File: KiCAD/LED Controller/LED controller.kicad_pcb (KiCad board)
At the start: 2 copper layers, 100 x 100 mm, 35 parts, among them J1 Barrel_Jack_Switch, J2 4x RJ45, SW1 ELUMOASAQ2C22, SW2 ELUMOASAQ2C22, SW3 ELUMOASAQ2C22, U1 SN75374D, U2 SN75374D, U3 Teensy4.1, U4 SN75374D, U5 SN74LV4053ADR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

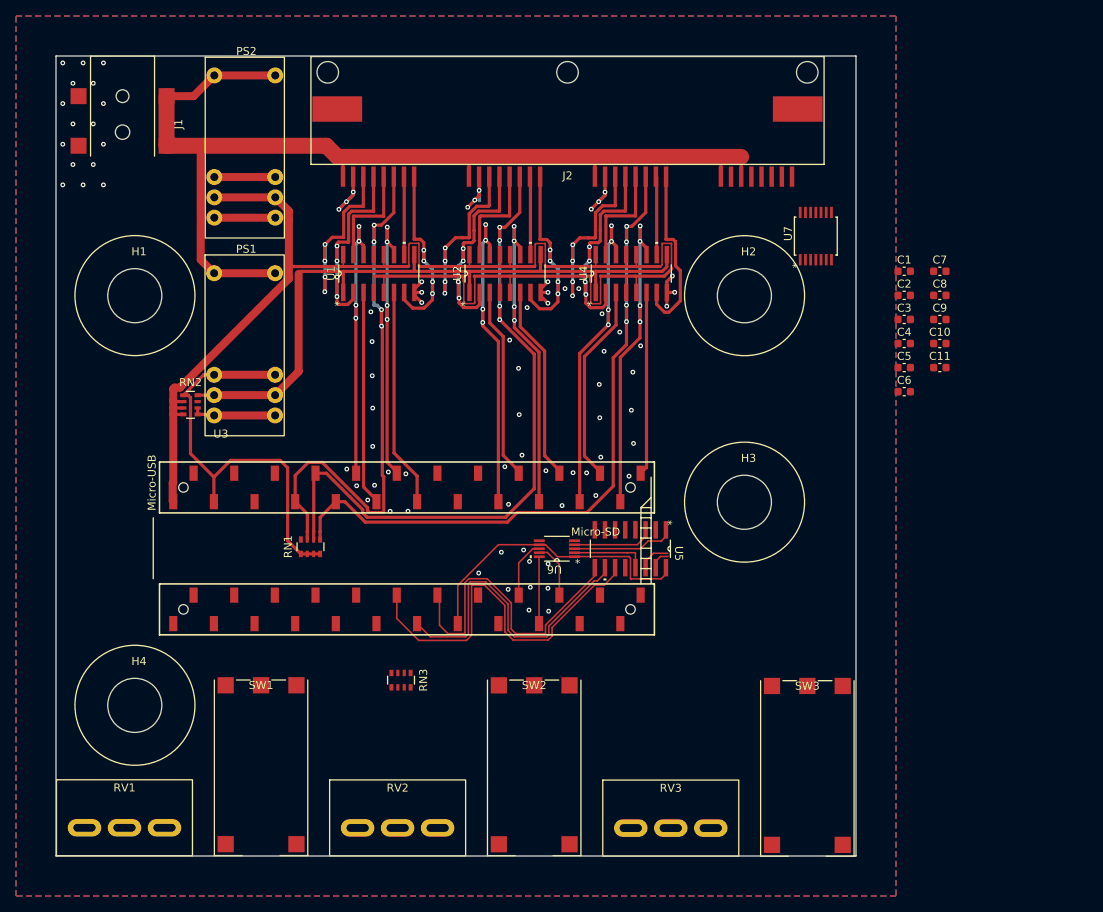
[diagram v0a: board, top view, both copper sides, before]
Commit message: Input jack added
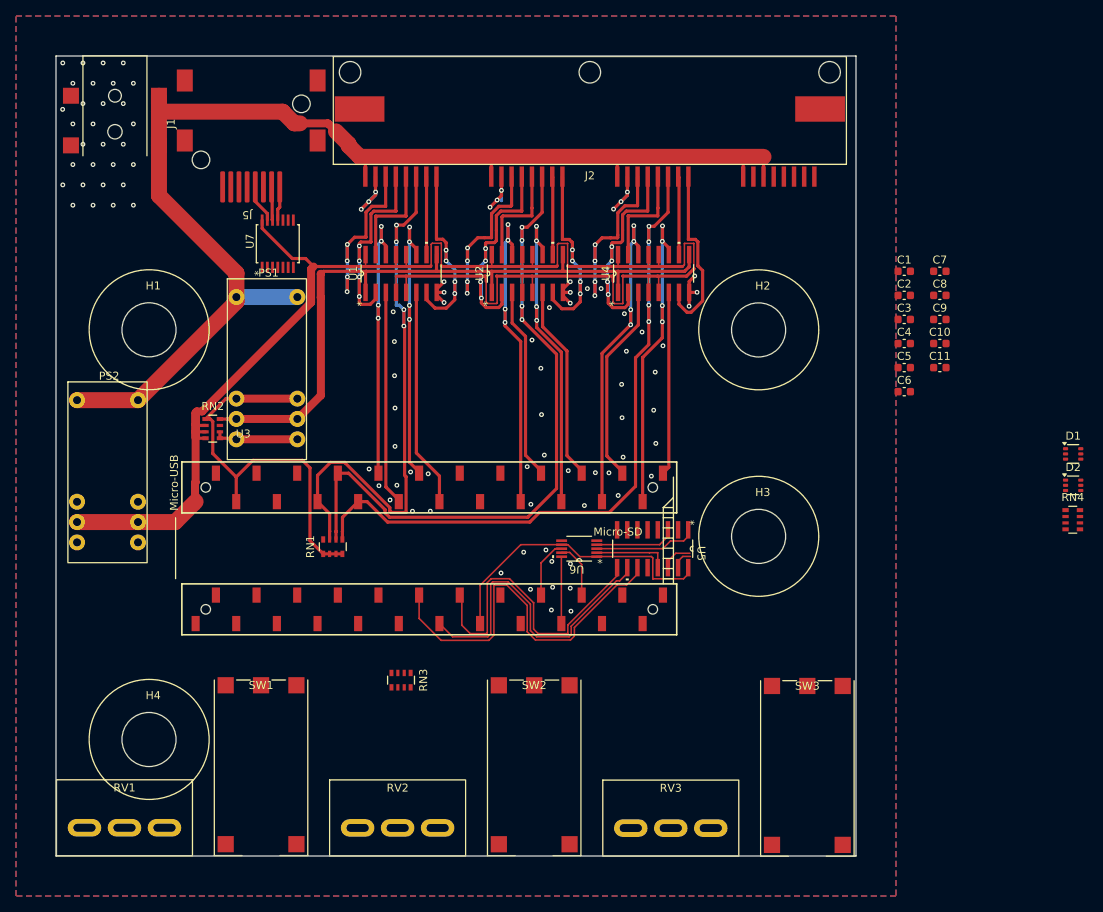
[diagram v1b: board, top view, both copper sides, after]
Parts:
- added D1: BAT54BRW, Package_TO_SOT_SMD:SOT-363_SC-70-6, F.Cu at (127.1, 49.7)
- added D2: BAT54BRW, Package_TO_SOT_SMD:SOT-363_SC-70-6, F.Cu at (127.1, 53.7)
- added J5: 8P8C_Shielded, Custom Footprints:1x RJ45, F.Cu at (24.4, 16.4)
- added RN4: 3600, Resistor_SMD:R_Array_Convex_4x0603, F.Cu at (127.1, 58.0)
- moved U7 67.3 mm to (27.7, 23.5)
- moved PS2 44.1 mm to (2.63, 43.0)
- moved H2 4.62 mm to (87.8, 34.2)
- moved H4 4.62 mm to (11.6, 85.4)
- moved H1 4.62 mm to (11.6, 34.2)
- moved H3 4.62 mm to (87.8, 60.0)
- moved PS1 4.08 mm to (22.6, 30.1)
- moved RN2 4.08 mm to (19.6, 46.6)
- moved J2 2.79 mm to (66.7, 16.3)
- moved U4 2.79 mm to (74.7, 27.2)
- moved RN1 2.79 mm to (34.6, 61.3)
- moved U1 2.79 mm to (43.1, 27.2)
- moved U2 2.79 mm to (58.9, 27.2)
- moved U3 2.79 mm to (46.7, 69.2)
- moved U6 2.79 mm to (65.4, 61.6)
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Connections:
- J2 pad 25: /12V -> /in1
- J2 pad 27: /12V -> /in2
- J2 pad 29: /Fan_PWM1 -> /in3
- J2 pad 31: /Fan_PWM2 -> /in4
- J2 pad 32: /Fan_PWM3 -> GND
- U3 pad 21: /SW1 -> /SW2
- U3 pad 22: /SW2 -> /SW3
- U3 pad 23: /SW3 -> /A-D_input_1
- U3 pad 24: /Ctrl_off -> /A-D_input_2
- U3 pad 25: /Ch3d -> Net-(U3-33_MCLK2)
- U3 pad 26: /Ch3c -> /A-D_input_3
- U3 pad 27: /Ch3b -> /Ch3d
- U3 pad 28: /Ch3a -> /Ch3c
- U3 pad 29: /Ch2d -> /Ch3b
- U3 pad 30: /Ch2c -> /Ch3a
- U3 pad 31: /Ch2b -> /Ch2d
- U3 pad 32: /Ch2a -> /Ch2c
- U3 pad 33: Net-(U3-41_A17) -> /Ch2b
- U3 pad 35: Net-(U3-13_SCK_LED) -> /Ch2a
- U3 pad 7: /Fan_enable -> /SW1
- U5 pad 6: /Ctrl_off -> GND
- U7 pad 8: /Fan_enable -> /3v3
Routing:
- net /12V: track 132.7 -> 156.1 mm
- net GND: track 60.5 -> 45.2 mm, vias 82 -> 96
- net /5V: track 197.6 -> 208.5 mm
- net /Fan_PWM1: track 0.00 -> 4.78 mm
- net /Fan_PWM3: track 0.00 -> 4.26 mm
- net /Fan_PWM2: track 0.00 -> 4.20 mm
- net /18V: track 87.5 -> 90.5 mm
- net /3v3: track 89.3 -> 86.4 mm

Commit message: Add I/O jack, and re-route
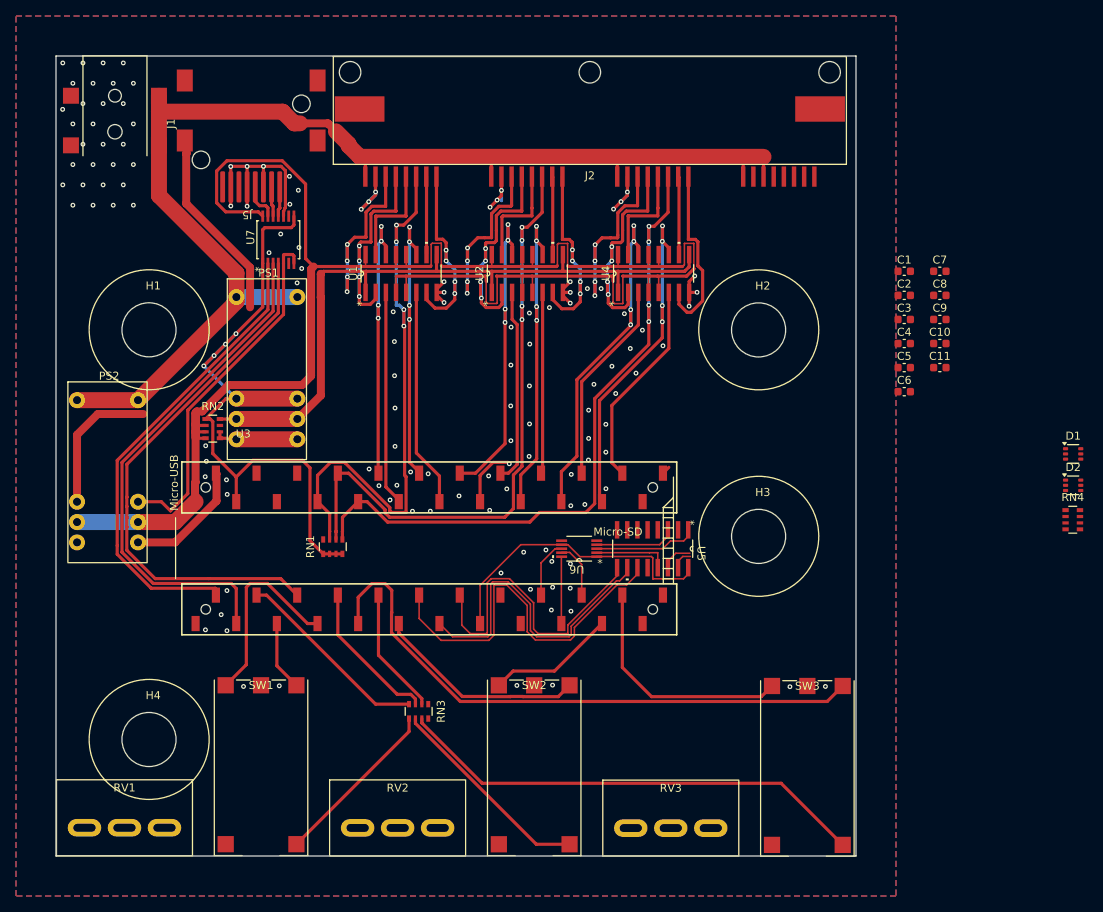
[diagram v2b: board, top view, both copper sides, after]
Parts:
- moved RN3 4.48 mm to (45.3, 81.9)
- moved U7 0.50 mm to (27.8, 23.0)
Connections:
- U3 pad 10: /SW1 red -> /SW3 red
- U3 pad 4: /SW3 red -> /SW1 red
- U3 pad 5: /SW3 green -> /SW1 green
- U3 pad 9: /SW1 green -> /SW3 green
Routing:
- net GND: track 45.2 -> 182.3 mm, vias 96 -> 133
- net /SW3 green: track 0.00 -> 74.6 mm
- net /Fan_PWM3_low: track 0.00 -> 67.3 mm
- net /Fan_PWM2_low: track 0.00 -> 64.5 mm
- net Net-(RN3-R2.2): track 0.00 -> 59.5 mm
- net /Fan_PWM1_low: track 0.00 -> 59.1 mm
- net /3v3: track 86.4 -> 123.2 mm, vias 0 -> 4
- net /5V: track 208.5 -> 238.5 mm
- net /SW3: track 0.00 -> 29.8 mm
- net /SW2 green: track 0.00 -> 26.5 mm
- net Net-(RN3-R3.2): track 0.00 -> 26.1 mm
- net /SW1 red: track 0.00 -> 24.7 mm
- net /SW1: track 0.00 -> 24.5 mm
- net Net-(RN3-R4.2): track 0.00 -> 21.5 mm
- net /SW2 red: track 0.00 -> 18.6 mm
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
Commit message: more traces added - better grounding
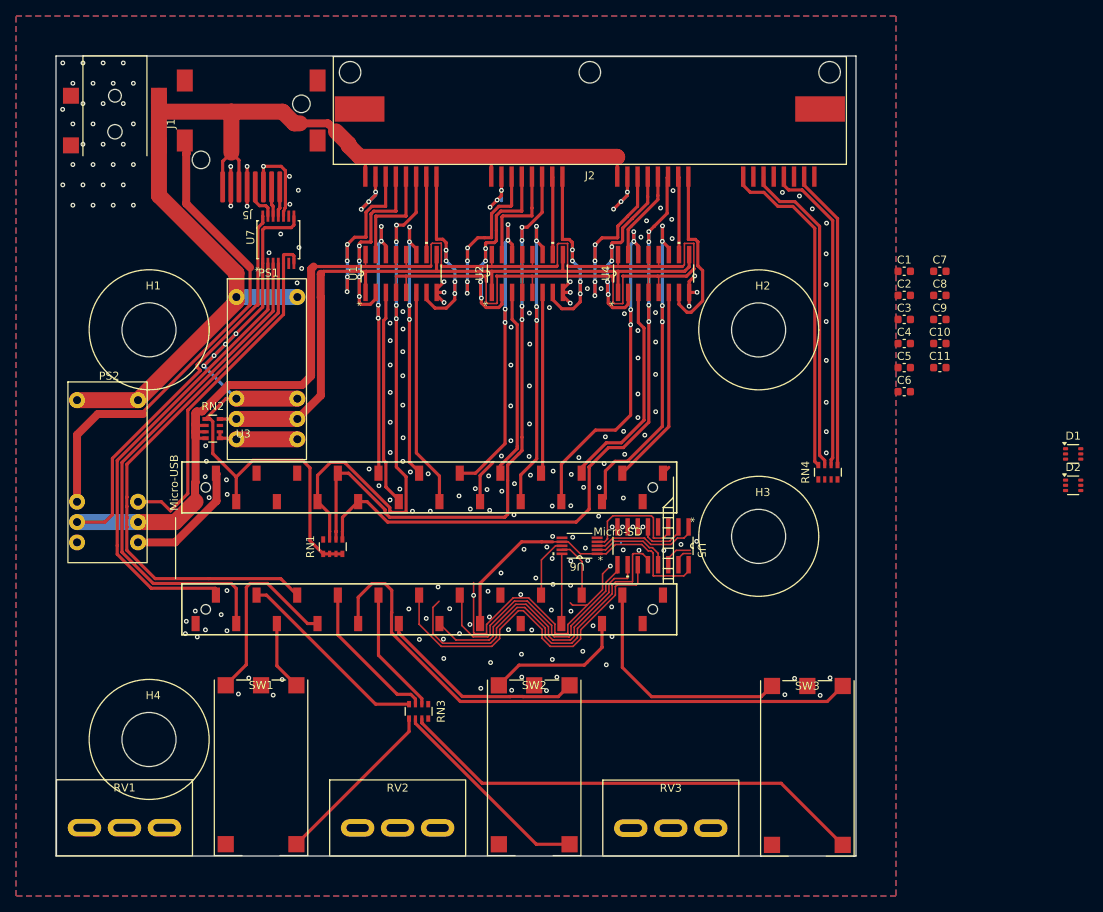
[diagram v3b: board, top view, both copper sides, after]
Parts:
- moved RN4 31.2 mm to (96.5, 52.0), turned to 90 degrees
- moved U5 0.37 mm to (74.6, 61.2)
- moved U6 0.37 mm to (65.4, 61.2)
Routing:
- net GND: track 182.3 -> 284.6 mm, vias 133 -> 219
- net /in1: track 0.00 -> 42.0 mm
- net /in2: track 0.00 -> 40.3 mm
- net /in3: track 0.00 -> 39.7 mm
- net /in4: track 0.00 -> 37.8 mm
- net /5V: track 238.5 -> 254.8 mm
- net /12V: track 156.1 -> 146.1 mm
- net /Ana3: track 10.1 -> 16.0 mm
- net /LED_PWM3: track 38.9 -> 34.7 mm
- net /LED_PWM2: track 40.1 -> 36.4 mm
- net /LED_PWM1: track 47.5 -> 44.0 mm
- net /Ana2: track 13.8 -> 16.2 mm
- net /3-1: track 13.5 -> 11.3 mm
- net /SW2: track 16.1 -> 17.9 mm
- net /Ch3b: track 25.5 -> 27.2 mm
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
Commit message: All but caps connected
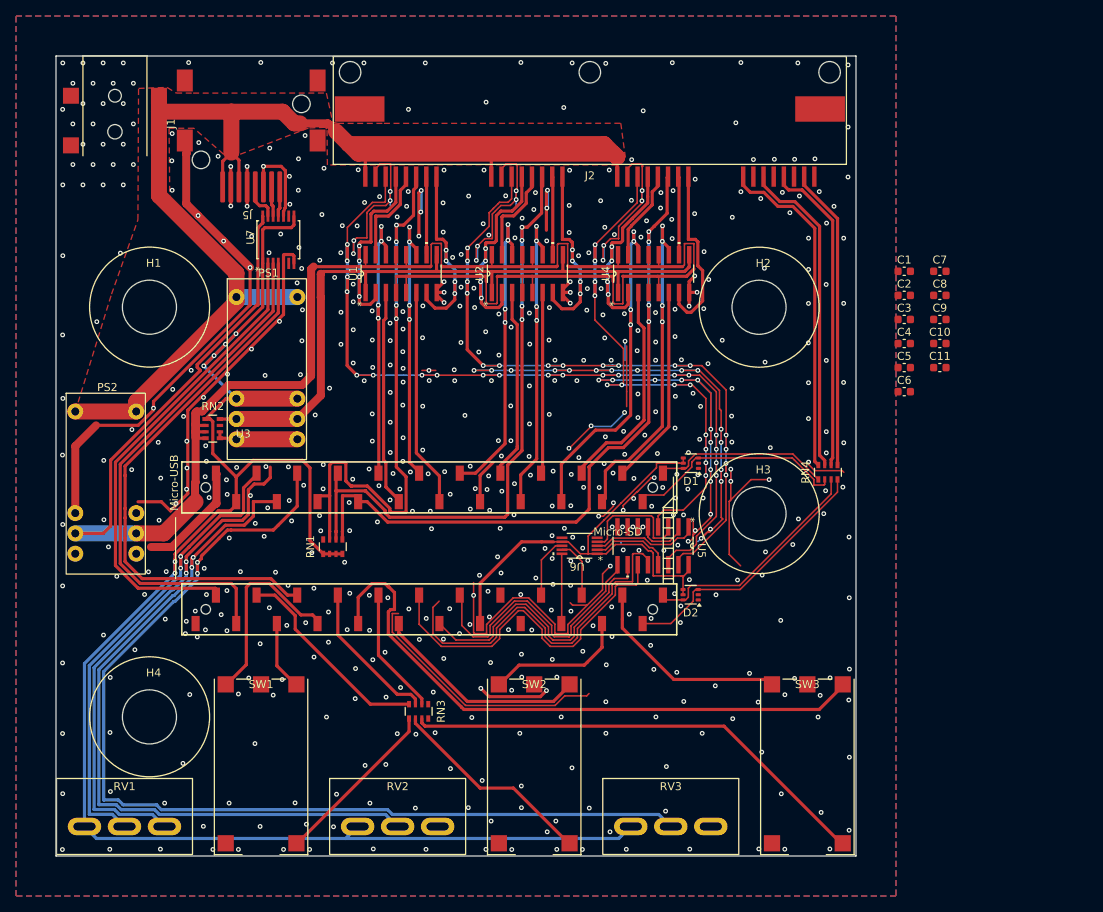
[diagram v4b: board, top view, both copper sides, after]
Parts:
- moved D2 49.7 mm to (79.3, 67.3), turned to 180 degrees
- moved D1 47.8 mm to (79.4, 50.9), turned to 180 degrees
- moved H2 2.83 mm to (87.9, 31.4)
- moved H4 2.83 mm to (11.7, 82.6)
- moved H1 2.83 mm to (11.7, 31.4)
- moved H3 2.83 mm to (87.9, 57.2)
- moved PS2 1.43 mm to (2.41, 44.4)
- moved RV3 0.20 mm to (76.8, 96.3)
- moved SW3 0.20 mm to (93.9, 88.9)
- moved RV2 0.18 mm to (42.7, 96.3)
- moved RV1 0.16 mm to (8.56, 96.3)
- moved SW2 0.12 mm to (59.8, 88.9)
- moved SW1 0.11 mm to (25.6, 88.9)
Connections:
- D1 pad 3: /A-D_input_1 -> /A-D_input_2
- D1 pad 4: /3.3V -> /3v3
- D1 pad 5: /3.3V -> /3v3
- D1 pad 6: /A-D_input_3 -> /A-D_input_1
- D2 pad 3: /A-D_input_2 -> /A-D_input_4
- D2 pad 4: /3.3V -> /3v3
- D2 pad 5: /3.3V -> /3v3
- D2 pad 6: /A-D_input_4 -> /A-D_input_3
- U3 pad 23: /A-D_input_1 -> /A-D_input_4
- U3 pad 24: /A-D_input_2 -> /A-D_input_3
- U3 pad 25: Net-(U3-33_MCLK2) -> /A-D_input_1
- U3 pad 26: /A-D_input_3 -> /A-D_input_2
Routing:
- net GND: track 284.6 -> 622.7 mm, vias 219 -> 619
- net /3v3: track 124.6 -> 268.7 mm, vias 4 -> 6
- net /Pot3: track 0.00 -> 128.0 mm, vias 0 -> 2
- net /Ctrl1: track 28.2 -> 120.1 mm, vias 4 -> 20
- net /Pot2: track 0.00 -> 90.5 mm, vias 0 -> 2
- net /Ctrl2: track 24.4 -> 101.4 mm, vias 4 -> 16
- net /Pot1: track 0.00 -> 59.3 mm, vias 0 -> 2
- net /Ctrl3: track 22.0 -> 73.9 mm, vias 4 -> 12
- net /12V: track 146.1 -> 181.7 mm
- net /A-D_input_4: track 0.00 -> 33.4 mm
- net /A-D_input_3: track 0.00 -> 29.4 mm
- net /A-D_input_2: track 0.00 -> 28.1 mm
- net /A-D_input_1: track 0.00 -> 22.3 mm
- net /SW3: track 29.8 -> 25.8 mm
- net /Temp3: track 86.3 -> 88.8 mm
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- added copper zone on F.Cu, net /12V

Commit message: All connected - pass DRC
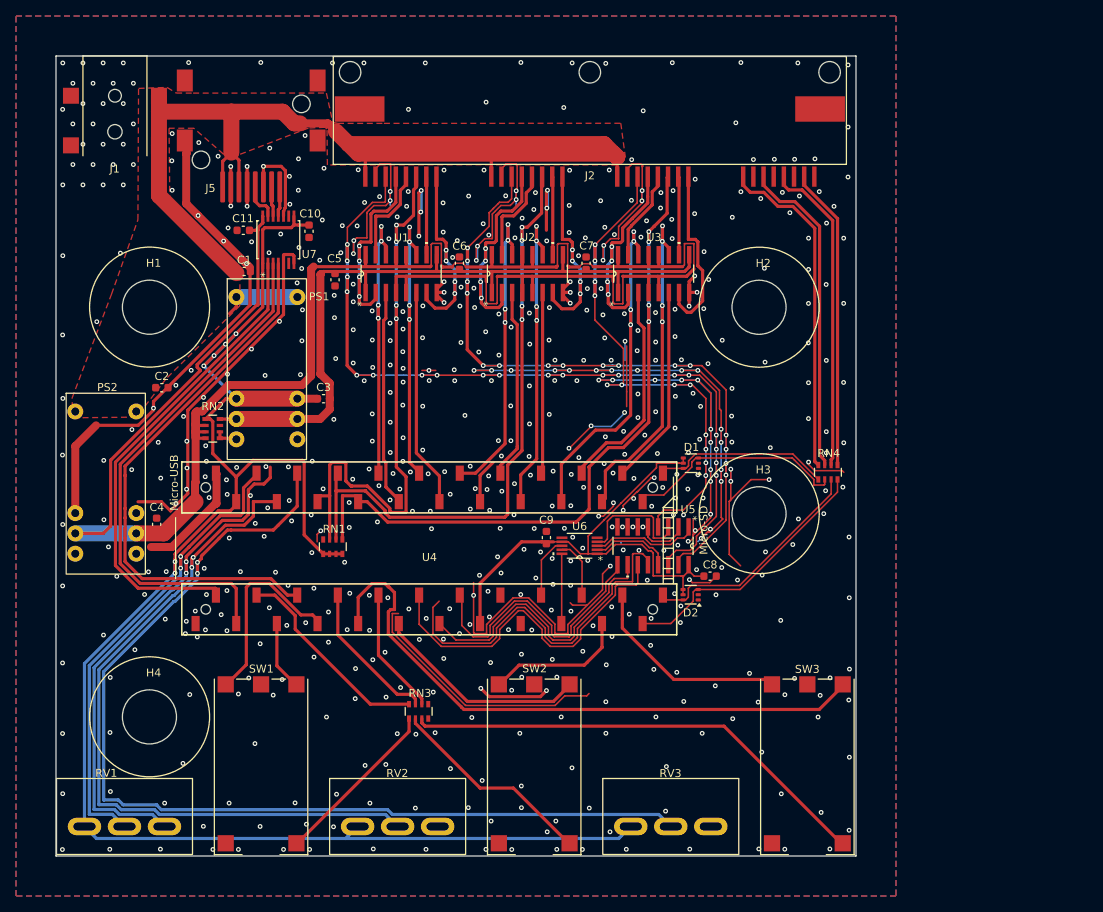
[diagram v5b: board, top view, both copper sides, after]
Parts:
- moved C4 96.1 mm to (12.6, 58.5), turned to -90 degrees
- moved C2 93.5 mm to (13.2, 41.5)
- moved C11 88.7 mm to (23.4, 21.8), turned to 180 degrees
- moved C1 82.5 mm to (23.5, 26.9)
- moved C10 80.1 mm to (31.6, 21.9), turned to -90 degrees
- moved C3 73.3 mm to (33.4, 42.8)
- moved C5 72.0 mm to (34.9, 28.0), turned to -90 degrees
- moved C6 57.9 mm to (50.4, 25.9), turned to 90 degrees
- moved C9 56.2 mm to (61.3, 60.2), turned to 90 degrees
- moved C8 45.4 mm to (81.8, 65.0)
- moved C7 44.2 mm to (66.3, 25.9), turned to 90 degrees
- renumbered U4 to U3, U3 to U4
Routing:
- net /12V: track 181.7 -> 154.0 mm
- net /3v3: track 268.7 -> 276.0 mm
- net /18V: track 90.5 -> 93.1 mm
- net GND: track 622.7 -> 620.5 mm, vias 619 -> 620
- net /5V: track 256.9 -> 258.9 mm

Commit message: Better 18V cap placement
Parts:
- moved C6 15.1 mm to (65.5, 27.5), turned to -90 degrees
- moved C5 14.5 mm to (49.4, 27.5)
- moved C7 14.5 mm to (80.7, 26.4), turned to -90 degrees
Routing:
- net /2-4: track 25.1 -> 27.5 mm
- net /1-4: track 25.0 -> 27.2 mm
- net /18V: track 93.1 -> 94.7 mm
- net /3-4: track 22.2 -> 23.6 mm
- net /5V: track 258.9 -> 260.0 mm
- net GND: vias 620 -> 617

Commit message: Labels added
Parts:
- added SYM1: Logo_Open_Hardware_Small, Custom Footprints:CC-BY-SA Symbol, F.Cu at (61.6, 41.6)
- added SYM2: Logo_Open_Hardware_Small, Symbol:OSHW-Logo_5.7x6mm_SilkScreen, F.Cu at (53.2, 42.5)
- added SYM3: Logo_Center_Positive, Custom Footprints:Polarity, F.Cu at (7.43, 18.8)
- moved C6 0.32 mm to (65.2, 27.5)
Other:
- board text added: "12V DC"
- board text added: "30 mm Cage Plate LED Controller"
- board text added: "Digital Inputs -14V/+17V Max"
- board text added: "Fans"
- board text added: "LED Board #1"
- board text added: "LED Board #2"
- board text added: "LED Board #3"
- board text added: "Teensy 4.1"
- board text added: "https://github.com/Llamero/30mm_cage_plate_LED_MCPCB Designer: Benjamin E. Smith, Funded by: NIH P30EY003176"
